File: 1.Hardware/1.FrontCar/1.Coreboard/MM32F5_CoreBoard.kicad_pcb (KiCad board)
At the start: 4 copper layers, 47.5 x 30.9 mm, 86 parts, among them J1 IPS114, J3 BTB_02x30, J4 BTB_02x30, J5 SH1.0_4P, J7 SH1.0_2P, SW1 3x4, SW2 3x4, SW3 3x4, SW4 3x4, U1 RT9013-33GB, U3 SN65HVD232, U4 SN65HVD232, U5 MM32F5277E9P, U6 MPU-6050, Y1 32.768KHz, Y2 8MHz

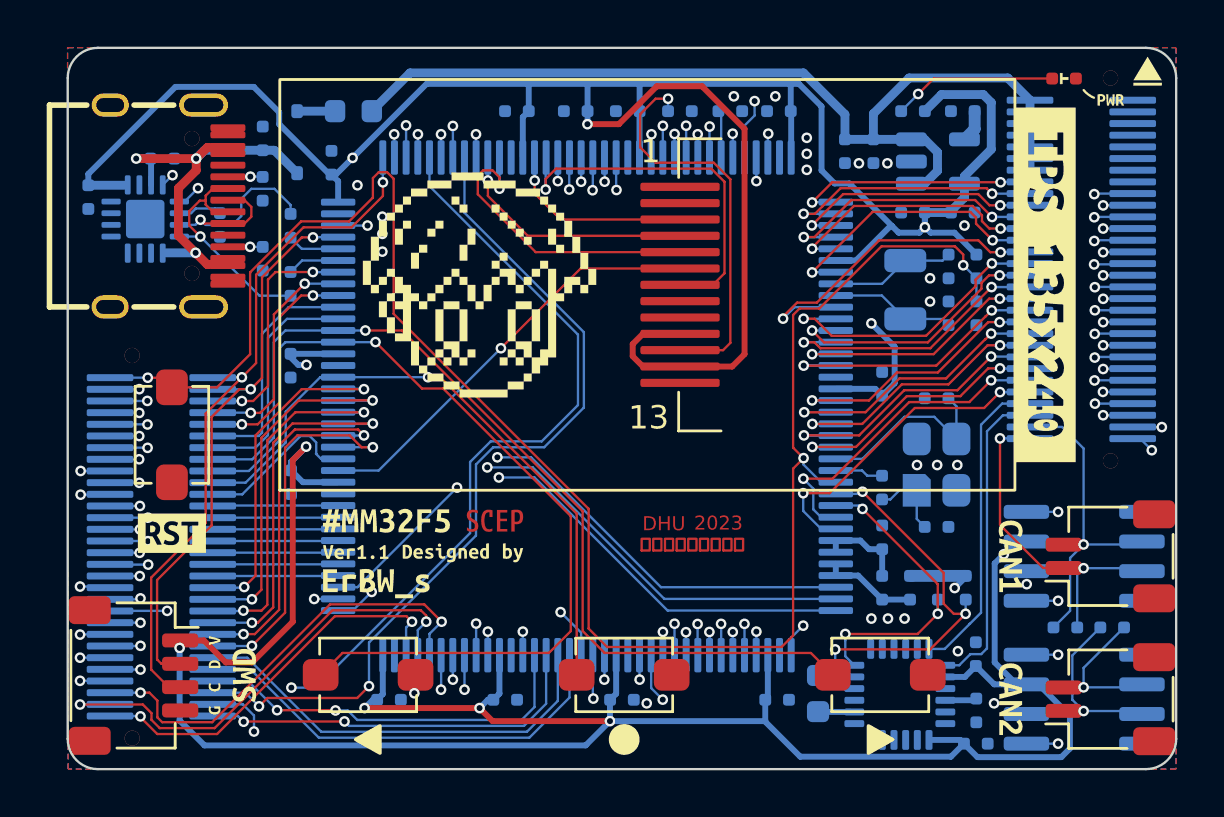
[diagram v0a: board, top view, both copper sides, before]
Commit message: 核心板v1.1，EasyUI初步实现
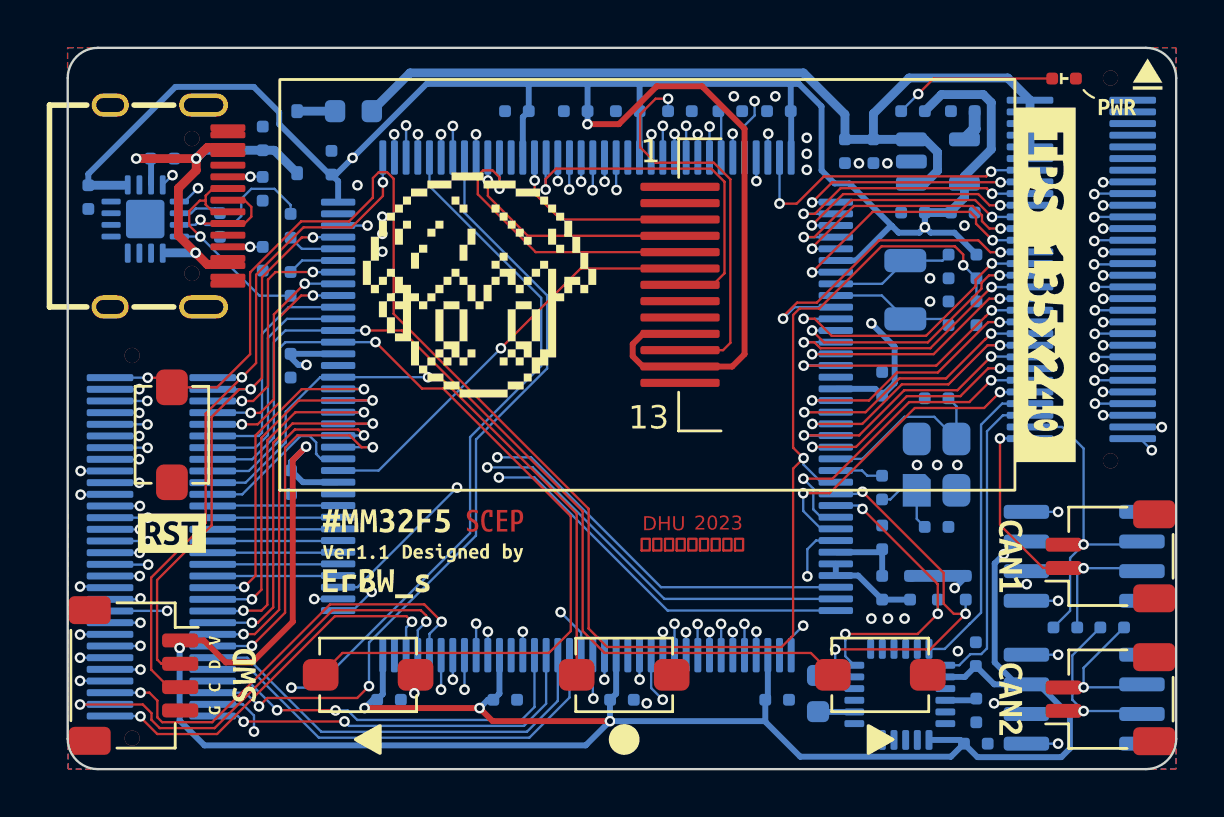
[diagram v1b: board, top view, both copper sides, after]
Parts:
- removed kibuzzard-63AB10B9: G***, kibuzzard-63AB10B9
- added kibuzzard-63BA4A79: G***, kibuzzard-63BA4A79, F.Cu at (121.2, 47.1)
- R1: value 5.1K -> 10R
- R4, R6: value 5.1K -> 4.7K
- R5: value 4.7K -> 10K
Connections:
- J3 pad 14: +5VA -> /PI1
- J3 pad 15: GND -> /PI0
- U5 pad 143: GND -> /PI1
- U5 pad 30: GNDA -> /PI0
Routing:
- net /PI0: track 0.00 -> 32.3 mm, vias 0 -> 2
- net /PI1: track 0.00 -> 13.3 mm, vias 0 -> 2
- net /CAM_TXD: track 37.9 -> 35.3 mm
- net /CAM_RXD: track 37.2 -> 34.6 mm
- net GNDA: track 3.78 -> 3.18 mm
- net /CAN1_R: track 35.8 -> 36.3 mm
- net /CAN1_D: track 40.7 -> 41.2 mm
